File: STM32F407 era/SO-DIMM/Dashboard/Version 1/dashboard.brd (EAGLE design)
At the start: 94.3 x 70.6 mm, 93 parts, among them J1 SO-DIMM-CPU, U1 CAT4238TD-GT3, U10 SN65HVD232D, U2 IRF9332PBF, U3 TPS54331D, X2 SM10B-SRSS-TB, X3 SM10B-SRSS-TB, X6 057-014-1

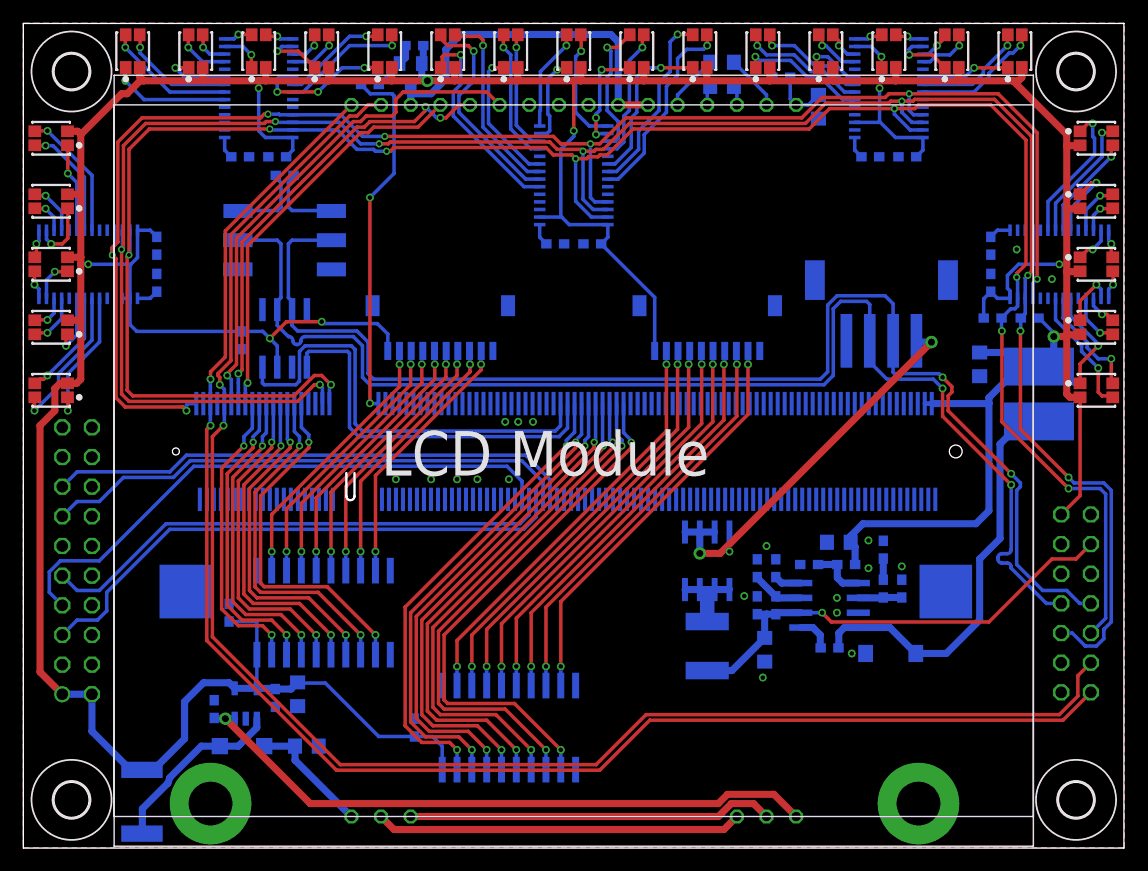
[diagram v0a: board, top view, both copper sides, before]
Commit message: update to dash, CPU. more work on COM-TC
- Dashboard
Fixed pinout error with overlapping interrupt pins.
Added missing silkscreen marking
- CPU
Added holes for mechanical fastening
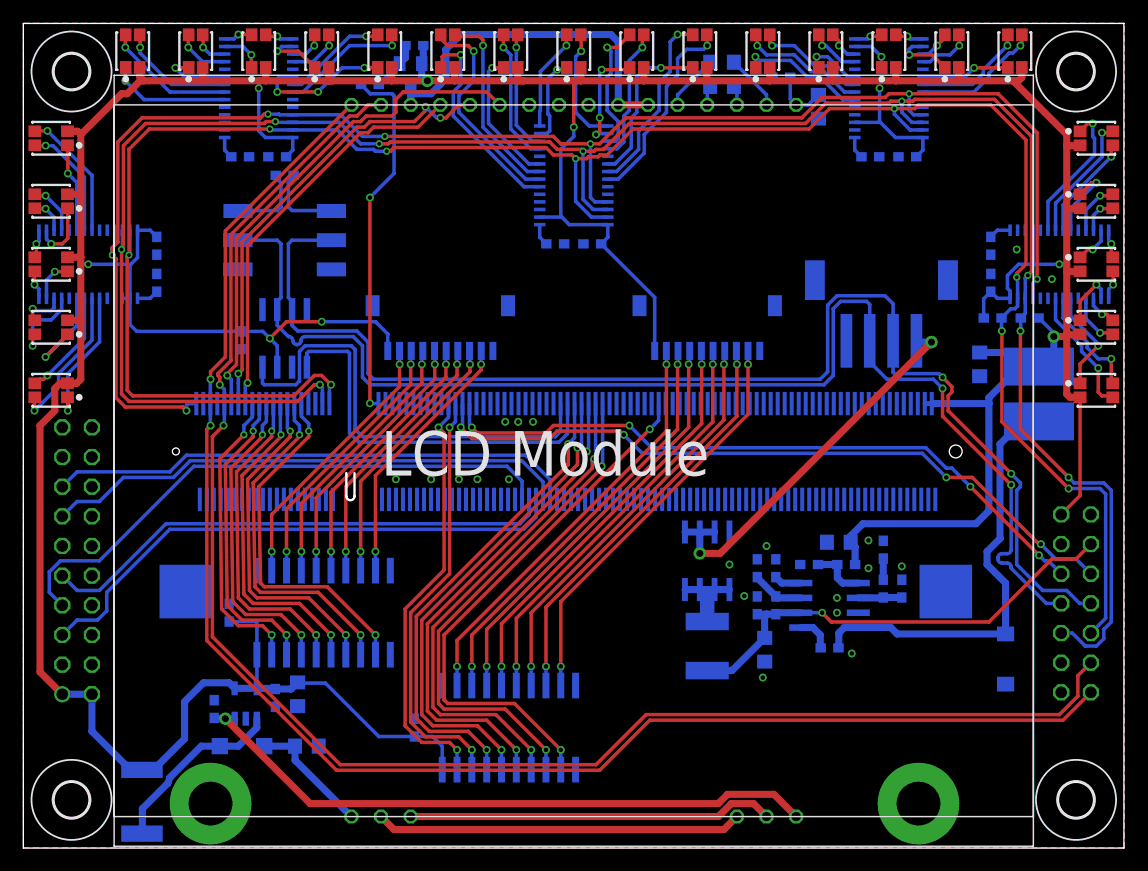
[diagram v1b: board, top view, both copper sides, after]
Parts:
- moved D2 9.85 mm to (84.1, 16.2), turned to 90 degrees
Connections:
- net BTN1: now also J1.61; no longer J1.97
- net BTN2: now also J1.63; no longer J1.99
- net BTN3: now also J1.97; no longer J1.101
- net BTN4: now also J1.99; no longer J1.103
- net BTN5: now also J1.101; no longer J1.105
- net BTN6: now also J1.103; no longer J1.107
- net BTN7: now also J1.105; no longer J1.109
- net BTN8: now also J1.121; no longer J1.111
- net DBG_RX: now also J1.67
- net DBG_TX: now also J1.65
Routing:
- net DBG_TX: track 0.00 -> 61.8 mm, vias 0 -> 4
- net DBG_RX: track 0.00 -> 58.3 mm, vias 0 -> 4
- net BTN2: track 41.3 -> 36.8 mm
- net BTN1: track 40.6 -> 36.5 mm
- net N$64: track 5.49 -> 8.85 mm
- net N$65: track 4.59 -> 6.81 mm
- net N$80: track 37.4 -> 39.3 mm
- net CAN_TX: track 32.7 -> 33.7 mm
- net CAN_RX: track 38.6 -> 39.6 mm
- net BTN7: track 44.9 -> 44.1 mm
- net 3.3V: track 416.9 -> 417.7 mm
- net BTN6: track 44.1 -> 43.4 mm
- net BTN8: track 45.8 -> 46.5 mm
- net N$66: track 3.18 -> 3.87 mm
- net BTN5: track 43.3 -> 42.7 mm

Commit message: more work on debug board silkscreen
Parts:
- R26: value 60 -> 120
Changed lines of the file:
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@@
 <attribute name="VALUE" x="21.66475" y="57.07" size="0.4064" layer="28" ratio="10" rot="MR90"/>
 </element>
-<element name="R26" library="microbuilder" package="_0603" value="60" x="22.38375" y="57.62625" smashed="yes" rot="MR180">
+<element name="R26" library="microbuilder" package="_0603" value="120" x="22.38375" y="57.62625" smashed="yes" rot="MR180">
 <attribute name="NAME" x="20.6375" y="56.99125" size="1.27" layer="26" font="vector" ratio="10" rot="MR0"/>
 <attribute name="VALUE" x="21.11375" y="59.11855" size="0.4064" layer="28" ratio="10" rot="MR180"/>

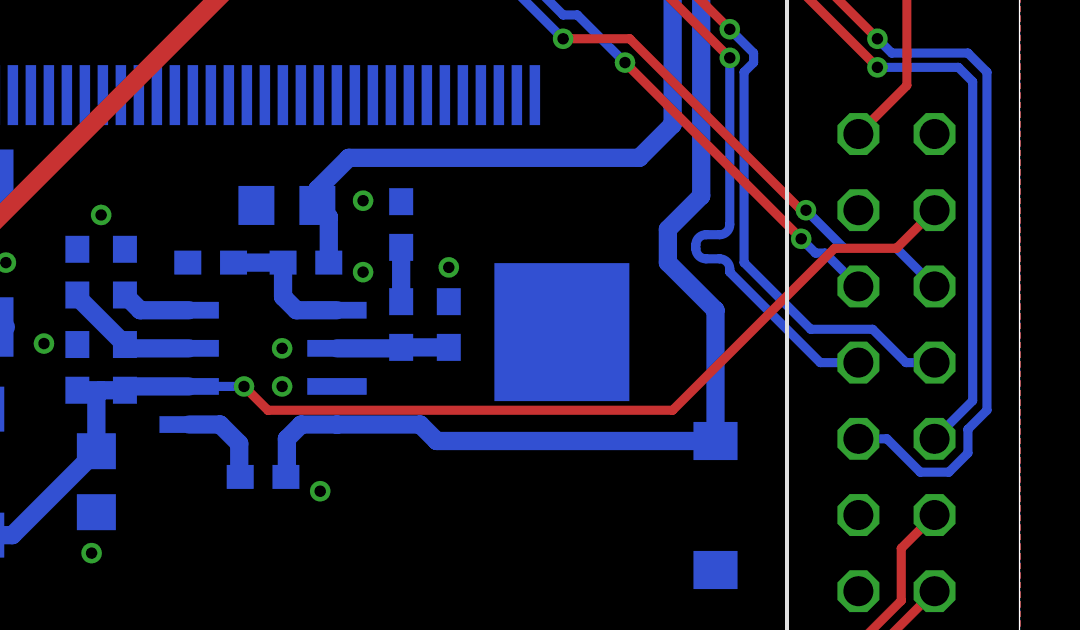
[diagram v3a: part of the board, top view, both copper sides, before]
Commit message: USB to UART done, mork work on COM/TC
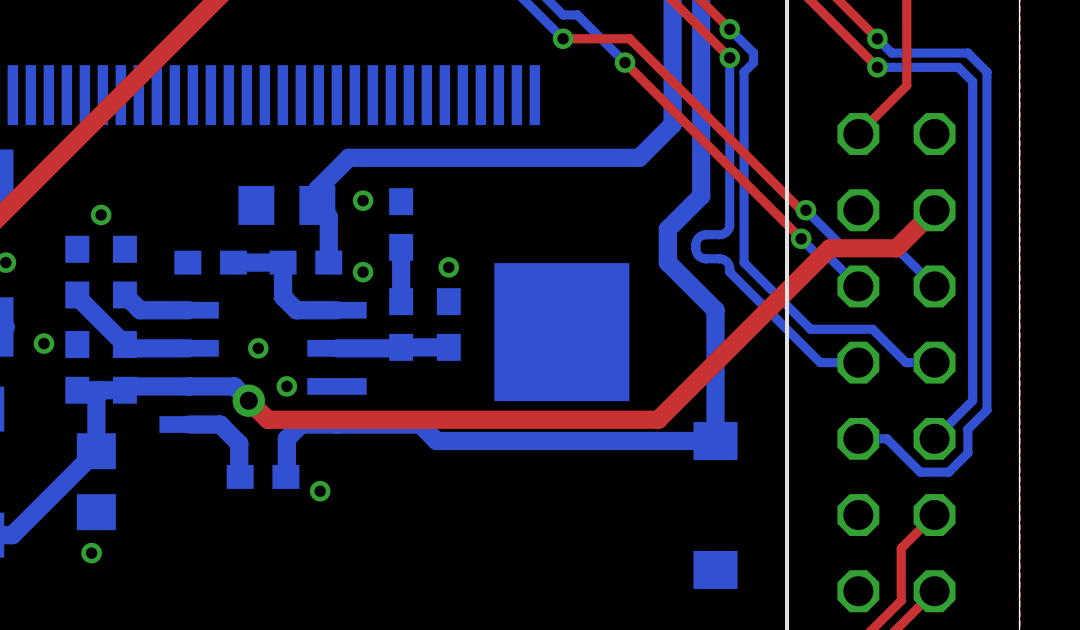
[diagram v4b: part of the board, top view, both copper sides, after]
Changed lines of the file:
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@@
 <via x="72.39" y="26.3525" extent="1-16" drill="0.381"/>
 <via x="72.39" y="23.97125" extent="1-16" drill="0.381"/>
-<via x="69.69125" y="20.16125" extent="1-16" drill="0.381"/>
-<via x="69.69125" y="21.43125" extent="1-16" drill="0.381"/>
+<via x="69.85" y="20.16125" extent="1-16" drill="0.381"/>
+<via x="68.8975" y="21.43125" extent="1-16" drill="0.381"/>
 <via x="75.2475" y="24.13" extent="1-16" drill="0.381"/>
 <via x="61.75375" y="21.59" extent="1-16" drill="0.381"/>
@@
 <wire x1="58.57875" y1="15.20375" x2="60.7015" y2="15.20375" width="0.6096" layer="16"/>
 <wire x1="60.7015" y1="15.20375" x2="63.5" y2="18.00225" width="0.6096" layer="16"/>
-<via x="68.42125" y="20.16125" extent="1-16" drill="0.381"/>
-<wire x1="68.42125" y1="20.16125" x2="69.215" y2="19.3675" width="0.3048" layer="1"/>
-<wire x1="82.70875" y1="19.3675" x2="88.10625" y2="24.765" width="0.3048" layer="1"/>
-<wire x1="88.10625" y1="24.765" x2="90.17" y2="24.765" width="0.3048" layer="1"/>
-<wire x1="90.17" y1="24.765" x2="91.44" y2="26.035" width="0.3048" layer="1"/>
-<wire x1="66.59245" y1="20.16125" x2="68.42125" y2="20.16125" width="0.3048" layer="16"/>
-<wire x1="69.215" y1="19.3675" x2="82.70875" y2="19.3675" width="0.3048" layer="1"/>
+<wire x1="66.59245" y1="20.16125" x2="68.10375" y2="20.16125" width="0.6096" layer="16"/>
+<wire x1="68.10375" y1="20.16125" x2="68.58" y2="19.685" width="0.6096" layer="16"/>
+<via x="68.58" y="19.685" extent="1-16" drill="0.6"/>
+<wire x1="68.58" y1="19.685" x2="69.215" y2="19.05" width="0.6096" layer="1"/>
+<wire x1="69.215" y1="19.05" x2="82.2325" y2="19.05" width="0.6096" layer="1"/>
+<wire x1="82.2325" y1="19.05" x2="87.9475" y2="24.765" width="0.6096" layer="1"/>
+<wire x1="90.17" y1="24.765" x2="91.44" y2="26.035" width="0.6096" layer="1"/>
+<wire x1="87.9475" y1="24.765" x2="90.17" y2="24.765" width="0.6096" layer="1"/>
 </signal>
 <signal name="N$77">

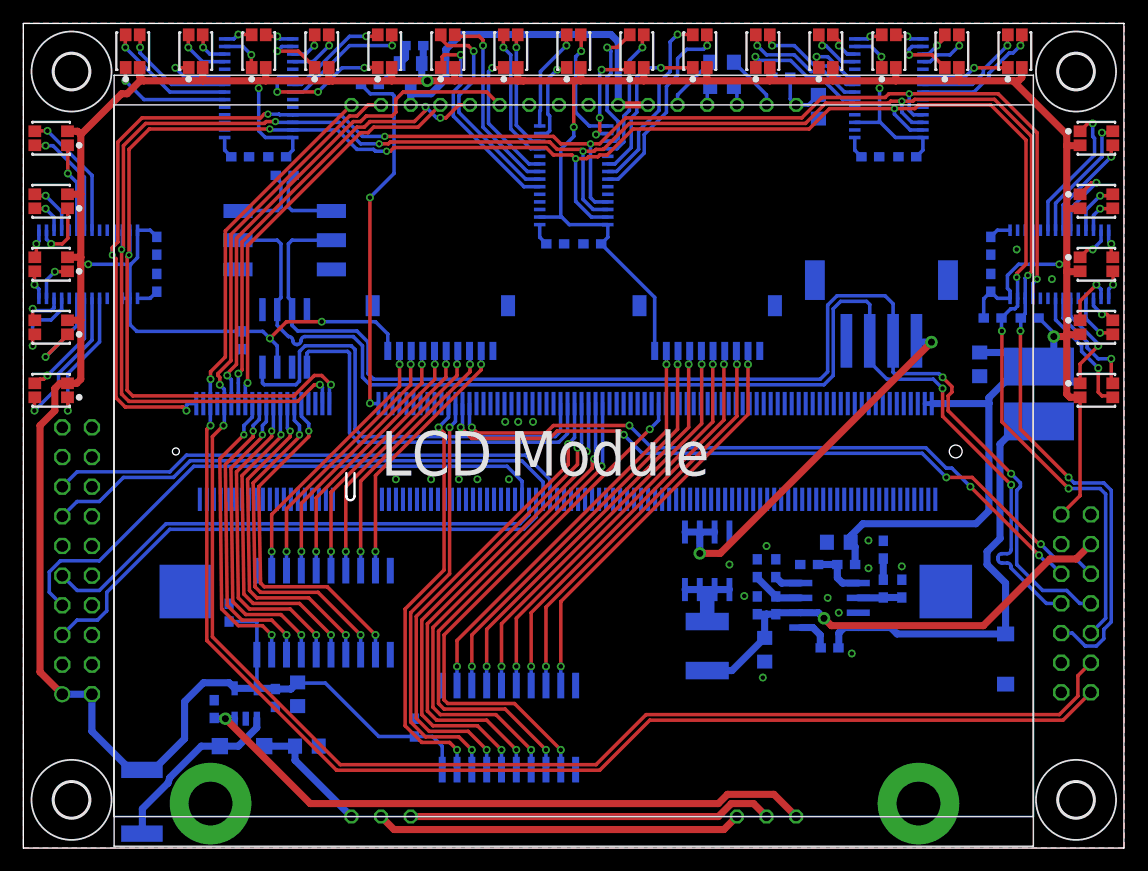
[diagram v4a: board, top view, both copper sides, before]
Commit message: last end changes on boards
Dev board
- Added 8 LED for ekstra debugging feature
- fixed Tvalue silkscreen
-

COM/TC
- fixed connections om P-channel RPP
- 12V from debug changed to include RPP and fuse

Dash
- fixed connections om P-channel RPP
- 12V from debug changed to include RPP and fuse

debug
- Added "ohm/not ohm to silkscreen
- Added BNC connectors for CAN

and much much more
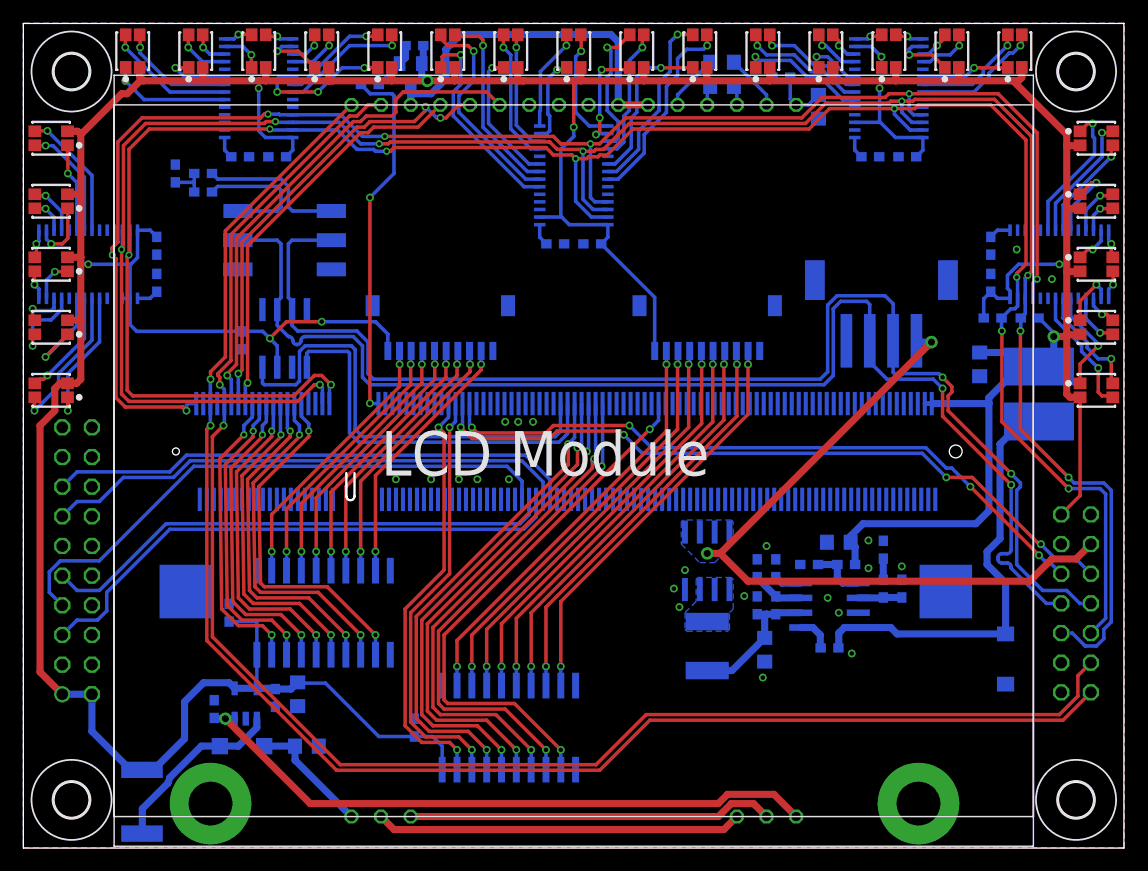
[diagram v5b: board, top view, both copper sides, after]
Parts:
- added C11: 47n, microbuilder:_0603
- added R11: 60, microbuilder:_0603
- R26: value 120 -> 60
- moved R26 6.99 mm to (15.4, 57.8)
- turned U2 to 90 degrees
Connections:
- new net N$119: R11.1, SW1.P$3
- net 12V: no longer X6.3
- net GND: now also C11.2
- net N$84: now also U2.1, U2.2, U2.3; no longer U2.5, U2.6, U2.7, U2.8
- net N$86: now also C11.1, R11.2; no longer SW1.P$3
- net VCC: now also U2.5, U2.6, U2.7, U2.8, X6.3; no longer U2.1, U2.2, U2.3
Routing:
- net VCC: track 33.0 -> 62.1 mm
- net 12V: track 40.2 -> 12.0 mm, vias 1 -> 0
- net N$119: track 0.00 -> 11.5 mm
- net N$84: track 11.1 -> 0.00 mm
- net N$85: track 6.71 -> 12.6 mm
- net N$86: track 6.71 -> 3.21 mm
- added copper zone on layer 16, net N$84
- added copper zone on layer 16, net VCC

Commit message: final changes
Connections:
- removed net N$104: U$5.2, X3.2
- removed net N$116: U$4.7, X2.7
- removed net N$117: U$4.8, X2.8
- removed net N$118: U$4.9, X2.9
- net BTN6: now also X2.7; no longer U$4.14
- net BTN7: now also X2.8; no longer U$4.13
- net BTN8: now also X2.9; no longer U$4.12
- net SW1: now also X3.2; no longer U$5.19
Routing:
- net N$116: track 35.5 -> 0.00 mm, vias 2 -> 0
- net N$117: track 35.5 -> 0.00 mm, vias 2 -> 0
- net N$118: track 35.3 -> 0.00 mm, vias 2 -> 0
- net BTN8: track 46.5 -> 19.9 mm
- net N$104: track 23.4 -> 0.00 mm, vias 2 -> 0
- net BTN7: track 44.1 -> 29.1 mm
- net BTN6: track 43.4 -> 28.9 mm
- net SW1: track 25.7 -> 21.5 mm
